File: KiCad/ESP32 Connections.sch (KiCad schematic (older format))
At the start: 1 part

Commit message: Analog inputs
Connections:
- net AI10: now also SPRKESP1.10 (DAC2/ADC2_9/GPIO26); no longer SPRKESP1.9 (DAC1/ADC2_8/GPIO25)
- net AI6: now also SPRKESP1.6 (Touch8/ADC1_5/GPIO33/XTAL32); no longer SPRKESP1.5 (Touch9/ADC1_4/GPIO32/XTAL32)
- net AI7: now also SPRKESP1.7 (VDETI/ADC1_6/GPI34); no longer SPRKESP1.6 (Touch8/ADC1_5/GPIO33/XTAL32)
- net AI8: now also SPRKESP1.8 (VDET2/ADC1_7/GPI35); no longer SPRKESP1.7 (VDETI/ADC1_6/GPI34)
- net AI9: now also SPRKESP1.9 (DAC1/ADC2_8/GPIO25); no longer SPRKESP1.8 (VDET2/ADC1_7/GPI35)
- new net AI5: SPRKESP1.5 (Touch9/ADC1_4/GPIO32/XTAL32)
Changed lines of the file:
@@
 LIBS:spark_esp32thing
 LIBS:HAP-IO-Card-cache
-EELAYER 25 0
+EELAYER 26 0
 EELAYER END
 $Descr A4 11693 8268
@@
 NoConn ~ 5400 4200
 $Comp
-L GND #PWR24
+L GND #PWR018
 U 1 1 5918208C
 P 5200 5900
-F 0 "#PWR24" H 5200 5650 50  0001 C CNN
+AR Path="/59181FE5/5918208C" Ref="#PWR018"  Part="1"
+AR Path="/59181FE5/59181FE5/5918208C" Ref="#PWR018"  Part="1"
+F 0 "#PWR018" H 5200 5650 50  0001 C CNN
 F 1 "GND" H 5200 5750 50  0000 C CNN
 F 2 "" H 5200 5900 50  0001 C CNN
@@
 NoConn ~ 5200 3800
 $Comp
-L GND #PWR19
+L GND #PWR019
 U 1 1 59182095
 P 5200 3600
-F 0 "#PWR19" H 5200 3350 50  0001 C CNN
+AR Path="/59181FE5/59182095" Ref="#PWR019"  Part="1"
+AR Path="/59181FE5/59181FE5/59182095" Ref="#PWR019"  Part="1"
+F 0 "#PWR019" H 5200 3350 50  0001 C CNN
 F 1 "GND" V 5200 3400 50  0000 C CNN
 F 2 "" H 5200 3600 50  0001 C CNN
@@
 $EndComp
 $Comp
-L GND #PWR22
+L GND #PWR020
 U 1 1 5918209B
 P 5200 4300
-F 0 "#PWR22" H 5200 4050 50  0001 C CNN
+AR Path="/59181FE5/5918209B" Ref="#PWR020"  Part="1"
+AR Path="/59181FE5/59181FE5/5918209B" Ref="#PWR020"  Part="1"
+F 0 "#PWR020" H 5200 4050 50  0001 C CNN
 F 1 "GND" V 5200 4100 50  0000 C CNN
 F 2 "" H 5200 4300 50  0001 C CNN
@@
 $EndComp
 $Comp
-L +3V3 #PWR18
+L +3V3 #PWR021
 U 1 1 591820A1
 P 5200 3500
-F 0 "#PWR18" H 5200 3350 50  0001 C CNN
+AR Path="/59181FE5/591820A1" Ref="#PWR021"  Part="1"
+AR Path="/59181FE5/59181FE5/591820A1" Ref="#PWR021"  Part="1"
+F 0 "#PWR021" H 5200 3350 50  0001 C CNN
 F 1 "+3V3" V 5200 3750 50  0000 C CNN
 F 2 "" H 5200 3500 50  0001 C CNN
@@
 U 1 1 591820B8
 P 5400 3900
+AR Path="/59181FE5/591820B8" Ref="SPRKESP1"  Part="1"
+AR Path="/59181FE5/59181FE5/591820B8" Ref="SPRKESP1"  Part="1"
 F 0 "SPRKESP1" H 5454 5520 60  0000 C CNN
 F 1 "Spark_ESP32Thing" H 5418 5100 60  0000 C CNN
@@
 $EndComp
 $Comp
-L +3V3 #PWR23
+L +3V3 #PWR022
 U 1 1 591840B8
 P 5200 4400
-F 0 "#PWR23" H 5200 4250 50  0001 C CNN
+AR Path="/59181FE5/591840B8" Ref="#PWR022"  Part="1"
+AR Path="/59181FE5/59181FE5/591840B8" Ref="#PWR022"  Part="1"
+F 0 "#PWR022" H 5200 4250 50  0001 C CNN
 F 1 "+3V3" V 5200 4650 50  0000 C CNN
 F 2 "" H 5200 4400 50  0001 C CNN
@@
 $EndComp
 $Comp
-L GND #PWR20
+L GND #PWR023
 U 1 1 59184108
 P 5200 3900
-F 0 "#PWR20" H 5200 3650 50  0001 C CNN
+AR Path="/59181FE5/59184108" Ref="#PWR023"  Part="1"
+AR Path="/59181FE5/59181FE5/59184108" Ref="#PWR023"  Part="1"
+F 0 "#PWR023" H 5200 3650 50  0001 C CNN
 F 1 "GND" V 5200 3700 50  0000 C CNN
 F 2 "" H 5200 3900 50  0001 C CNN
@@
 $EndComp
 $Comp
-L GND #PWR21
+L GND #PWR024
 U 1 1 59184116
 P 5200 4000
-F 0 "#PWR21" H 5200 3750 50  0001 C CNN
+AR Path="/59181FE5/59184116" Ref="#PWR024"  Part="1"
+AR Path="/59181FE5/59181FE5/59184116" Ref="#PWR024"  Part="1"
+F 0 "#PWR024" H 5200 3750 50  0001 C CNN
 F 1 "GND" V 5200 3800 50  0000 C CNN
 F 2 "" H 5200 4000 50  0001 C CNN
@@
 Text GLabel 5000 2300 0    60   Input ~ 0
 AI4
-Text GLabel 5200 2400 0    60   Input ~ 0
+Text GLabel 5000 2500 0    60   Input ~ 0
 AI6
-Text GLabel 5000 2500 0    60   Input ~ 0
+Text GLabel 5200 2600 0    60   Input ~ 0
 AI7
-Text GLabel 5200 2600 0    60   Input ~ 0
+Text GLabel 5000 2700 0    60   Input ~ 0
 AI8
 Wire Wire Line
@@
 Wire Wire Line
 	5000 2300 5200 2300
+Text GLabel 5200 2800 0    60   Input ~ 0
+AI9
+Text GLabel 5000 2900 0    60   Input ~ 0
+AI10
+Text GLabel 5200 2400 0    60   Input ~ 0
+AI5
 Wire Wire Line
-	5000 2500 5200 2500
-Text GLabel 4950 2700 0    60   Input ~ 0
-AI9
+	5200 2500 5000 2500
 Wire Wire Line
-	4950 2700 5200 2700
-Text GLabel 5200 2800 0    60   Input ~ 0
-AI10
+	5000 2700 5200 2700
+Wire Wire Line
+	5200 2900 5000 2900
 $EndSCHEMATC

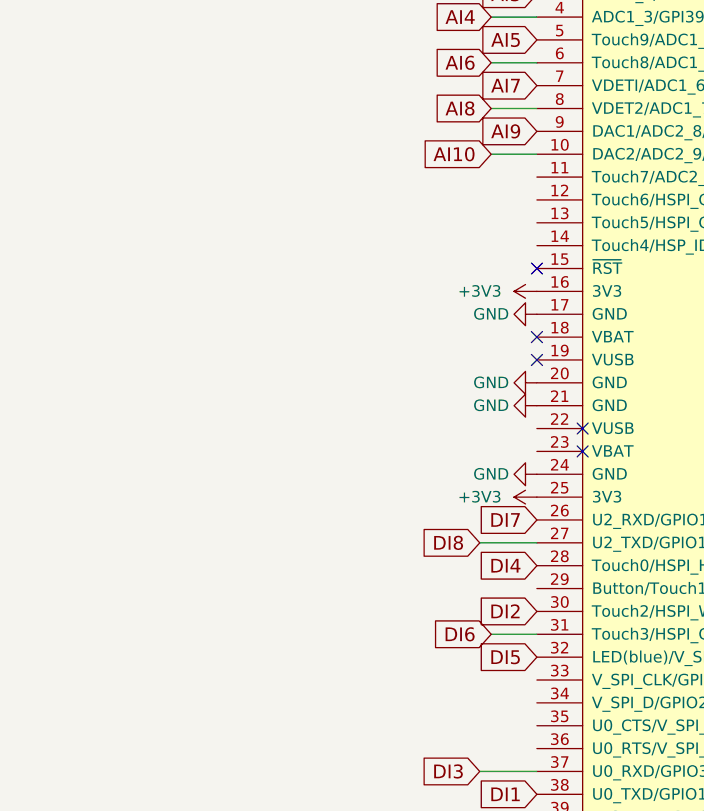
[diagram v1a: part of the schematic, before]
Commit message: Added power supply
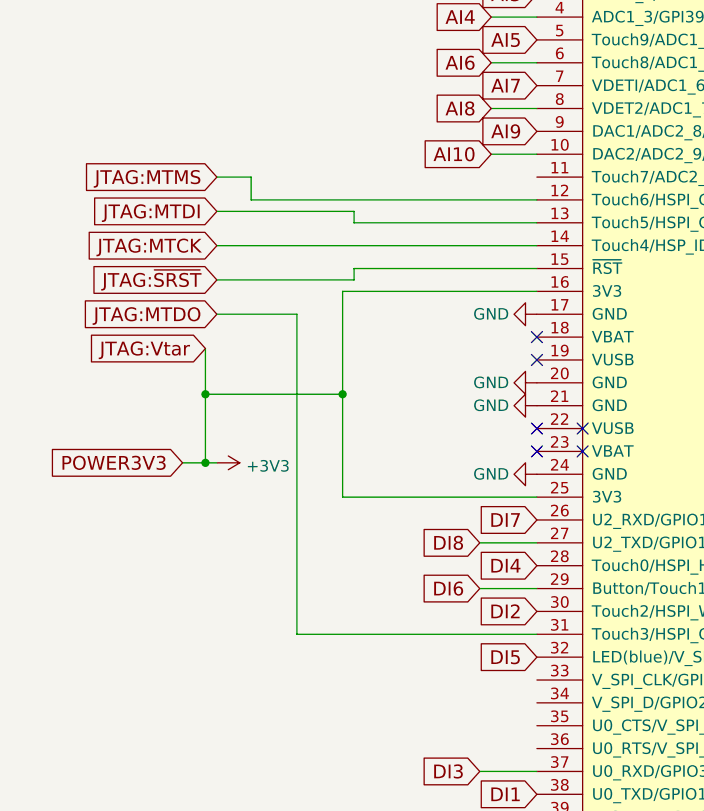
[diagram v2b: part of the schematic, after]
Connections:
- net DI6: now also SPRKESP1.29 (Button/Touch1/ADC2_1/GPIO0/CLK1); no longer SPRKESP1.31 (Touch3/HSPI_CS0/ADC2_3/GPIO15)
- net JTAG:MTMS: now reaches SPRKESP1.12 (Touch6/HSPI_CLK/ADC2_6/GPIO14)
- net JTAG:MTDI: now reaches SPRKESP1.13 (Touch5/HSPI_Q/ADC2_5/GPIO12)
- net JTAG:MTCK: now reaches SPRKESP1.14 (Touch4/HSP_ID/ADC2_4/GPIO13)
- net JTAG:~SRST: now reaches SPRKESP1.15 (~RST)
- new net JTAG:MTDO: SPRKESP1.31 (Touch3/HSPI_CS0/ADC2_3/GPIO15)
- no-connect marks 5 -> 6
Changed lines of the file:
@@
 LIBS:valves
 LIBS:spark_esp32thing
+LIBS:Power_Management
+LIBS:dc-dc
+LIBS:diode
+LIBS:ESD_Protection
+LIBS:SRR1260-330M
 LIBS:HAP-IO-Card-cache
 EELAYER 26 0
@@
 $Descr A4 11693 8268
 encoding utf-8
-Sheet 3 4
+Sheet 3 6
 Title ""
 Date ""
@@
 	0    1    1    0
 $EndComp
-NoConn ~ 5200 3400
 NoConn ~ 5200 3700
 NoConn ~ 5200 3800
@@
 $EndComp
 $Comp
-L +3V3 #PWR021
-U 1 1 591820A1
-P 5200 3500
-AR Path="/59181FE5/591820A1" Ref="#PWR021"  Part="1"
-AR Path="/59181FE5/59181FE5/591820A1" Ref="#PWR021"  Part="1"
-F 0 "#PWR021" H 5200 3350 50  0001 C CNN
-F 1 "+3V3" V 5200 3750 50  0000 C CNN
-F 2 "" H 5200 3500 50  0001 C CNN
-F 3 "" H 5200 3500 50  0001 C CNN
-	1    5200 3500
-	0    -1   -1   0
-$EndComp
-$Comp
 L Spark_ESP32Thing SPRKESP1
 U 1 1 591820B8
@@
 $EndComp
 $Comp
-L +3V3 #PWR022
-U 1 1 591840B8
-P 5200 4400
-AR Path="/59181FE5/591840B8" Ref="#PWR022"  Part="1"
-AR Path="/59181FE5/59181FE5/591840B8" Ref="#PWR022"  Part="1"
-F 0 "#PWR022" H 5200 4250 50  0001 C CNN
-F 1 "+3V3" V 5200 4650 50  0000 C CNN
-F 2 "" H 5200 4400 50  0001 C CNN
-F 3 "" H 5200 4400 50  0001 C CNN
-	1    5200 4400
-	0    -1   -1   0
-$EndComp
-$Comp
-L GND #PWR023
+L GND #PWR021
 U 1 1 59184108
 P 5200 3900
-AR Path="/59181FE5/59184108" Ref="#PWR023"  Part="1"
+AR Path="/59181FE5/59184108" Ref="#PWR021"  Part="1"
 AR Path="/59181FE5/59181FE5/59184108" Ref="#PWR023"  Part="1"
-F 0 "#PWR023" H 5200 3650 50  0001 C CNN
+F 0 "#PWR021" H 5200 3650 50  0001 C CNN
 F 1 "GND" V 5200 3700 50  0000 C CNN
 F 2 "" H 5200 3900 50  0001 C CNN
@@
 $EndComp
 $Comp
-L GND #PWR024
+L GND #PWR022
 U 1 1 59184116
 P 5200 4000
-AR Path="/59181FE5/59184116" Ref="#PWR024"  Part="1"
+AR Path="/59181FE5/59184116" Ref="#PWR022"  Part="1"
 AR Path="/59181FE5/59181FE5/59184116" Ref="#PWR024"  Part="1"
-F 0 "#PWR024" H 5200 3750 50  0001 C CNN
+F 0 "#PWR022" H 5200 3750 50  0001 C CNN
 F 1 "GND" V 5200 3800 50  0000 C CNN
 F 2 "" H 5200 4000 50  0001 C CNN
@@
 Text GLabel 5200 5100 0    60   Input ~ 0
 DI5
-Text GLabel 5000 5000 0    60   Input ~ 0
+Text GLabel 4950 4800 0    60   Input ~ 0
 DI6
 Text GLabel 5200 4500 0    60   Input ~ 0
@@
 Wire Wire Line
 	4950 4600 5200 4600
-Wire Wire Line
-	5200 5000 5000 5000
 Wire Wire Line
 	4950 5600 5200 5600
@@
 Wire Wire Line
 	5200 2900 5000 2900
+Text GLabel 3800 3150 0    60   Input ~ 0
+JTAG:MTDI
+Text GLabel 3800 3600 0    60   Input ~ 0
+JTAG:MTDO
+Text GLabel 3800 3300 0    60   Input ~ 0
+JTAG:MTCK
+Wire Wire Line
+	3800 3300 5200 3300
+Wire Wire Line
+	4950 4800 5200 4800
+Text GLabel 3800 3000 0    60   Input ~ 0
+JTAG:MTMS
+Wire Wire Line
+	3800 3150 4400 3150
+Wire Wire Line
+	4400 3150 4400 3200
+Wire Wire Line
+	4400 3200 5200 3200
+Wire Wire Line
+	5200 3100 3950 3100
+Wire Wire Line
+	3950 3100 3950 3000
+Wire Wire Line
+	3950 3000 3800 3000
+Wire Wire Line
+	4150 5000 5200 5000
+Wire Wire Line
+	4150 3600 3800 3600
+Text GLabel 3750 3750 0    60   Input ~ 0
+JTAG:Vtar
+Text GLabel 3800 3450 0    60   Input ~ 0
+JTAG:~SRST
+Wire Wire Line
+	3800 3450 4400 3450
+Wire Wire Line
+	4400 3450 4400 3400
+Wire Wire Line
+	4400 3400 5200 3400
+Wire Wire Line
+	4150 5000 4150 3600
+NoConn ~ 5200 4200
+NoConn ~ 5200 4100
+Text GLabel 3650 4250 0    60   Input ~ 0
+POWER3V3
+$Comp
+L +3V3 #PWR?
+U 1 1 591DFCE7
+P 3800 4250
+AR Path="/59181FE5/59181FE5/591DFCE7" Ref="#PWR?"  Part="1"
+AR Path="/59181FE5/591DFCE7" Ref="#PWR023"  Part="1"
+F 0 "#PWR023" H 3800 4100 50  0001 C CNN
+F 1 "+3V3" V 3815 4378 50  0000 L CNN
+F 2 "" H 3800 4250 50  0001 C CNN
+F 3 "" H 3800 4250 50  0001 C CNN
+	1    3800 4250
+	0    1    1    0
+$EndComp
+Wire Wire Line
+	5200 3500 4350 3500
+Wire Wire Line
+	4350 3500 4350 4400
+Wire Wire Line
+	4350 3950 3750 3950
+Connection ~ 3750 3950
+Wire Wire Line
+	4350 4400 5200 4400
+Connection ~ 4350 3950
+Wire Wire Line
+	3650 4250 3800 4250
+Wire Wire Line
+	3750 3750 3750 4250
+Connection ~ 3750 4250
 $EndSCHEMATC
